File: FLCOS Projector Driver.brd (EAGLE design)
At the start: 73.9 x 62.1 mm, 65 parts, among them IC2 LM3414, IC3 MIC5219BM5, IC4 MIC5219BM5, IC5 LM3414, IC6 LM3414, Q1 14.31818MHz, Q3 12MHz, T2 S8050, T3 S8050, U1 TVP5150-NTSC_DECODER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

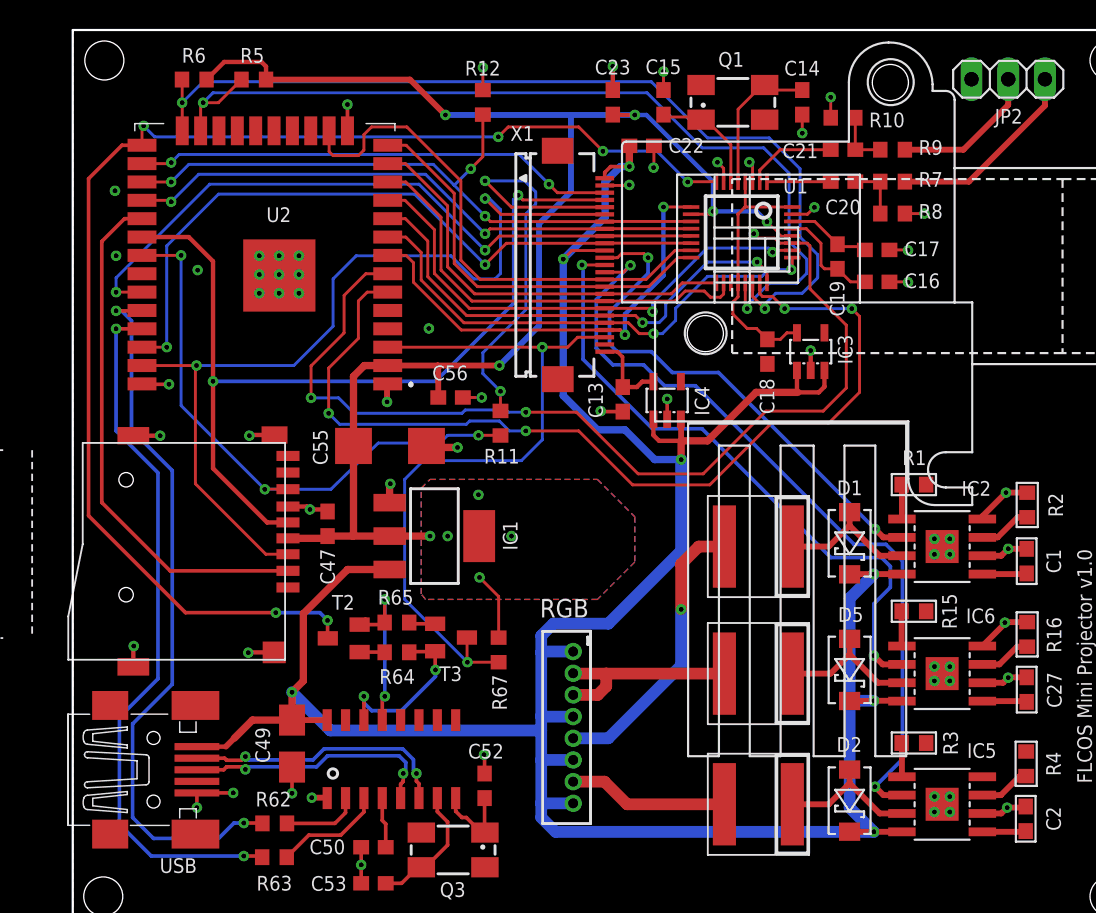
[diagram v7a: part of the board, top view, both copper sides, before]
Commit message: removed erroneous polys from tStop layer. Fixed 3V3 reg vias
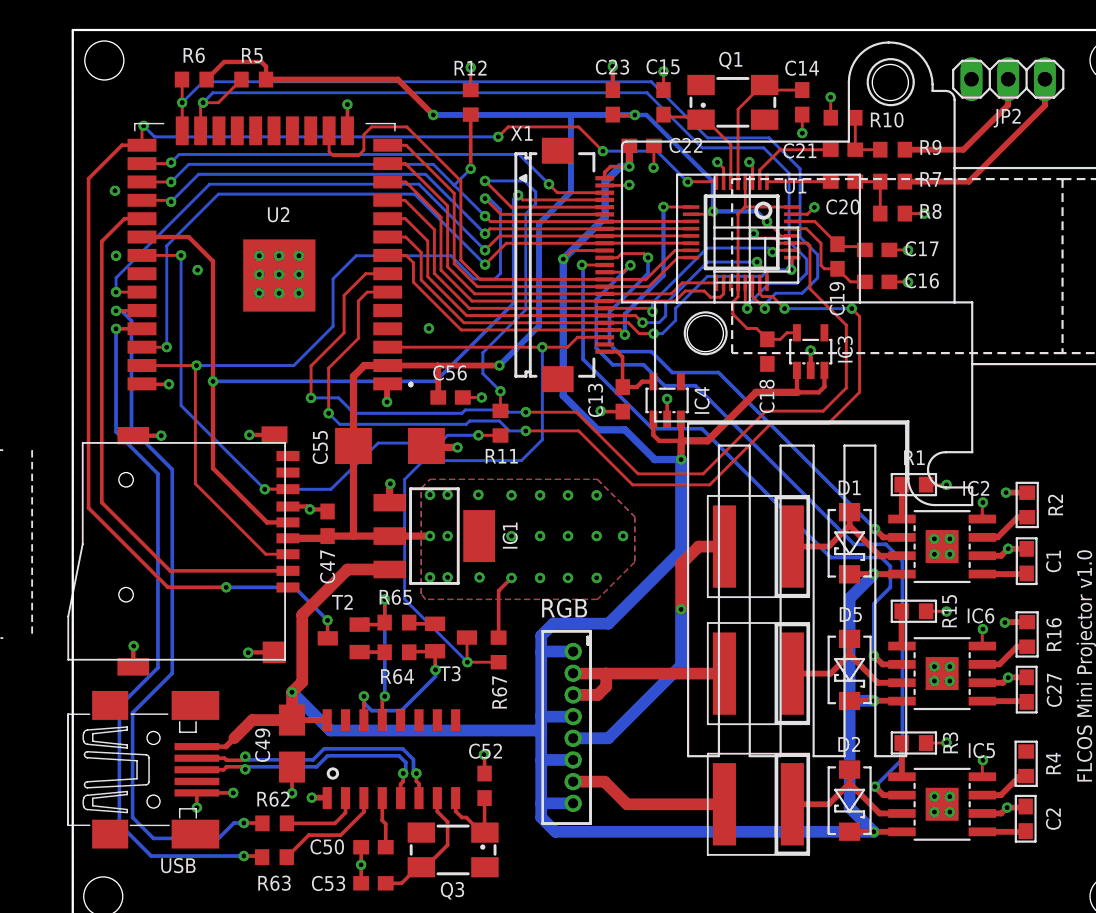
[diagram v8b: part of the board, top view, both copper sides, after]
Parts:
- moved R12 0.84 mm to (31.9, 60.9)
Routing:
- net GND: track 70.7 -> 74.0 mm, vias 63 -> 69
- net +3V3: track 108.7 -> 108.5 mm, vias 10 -> 26
